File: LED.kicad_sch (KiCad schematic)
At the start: 87 parts

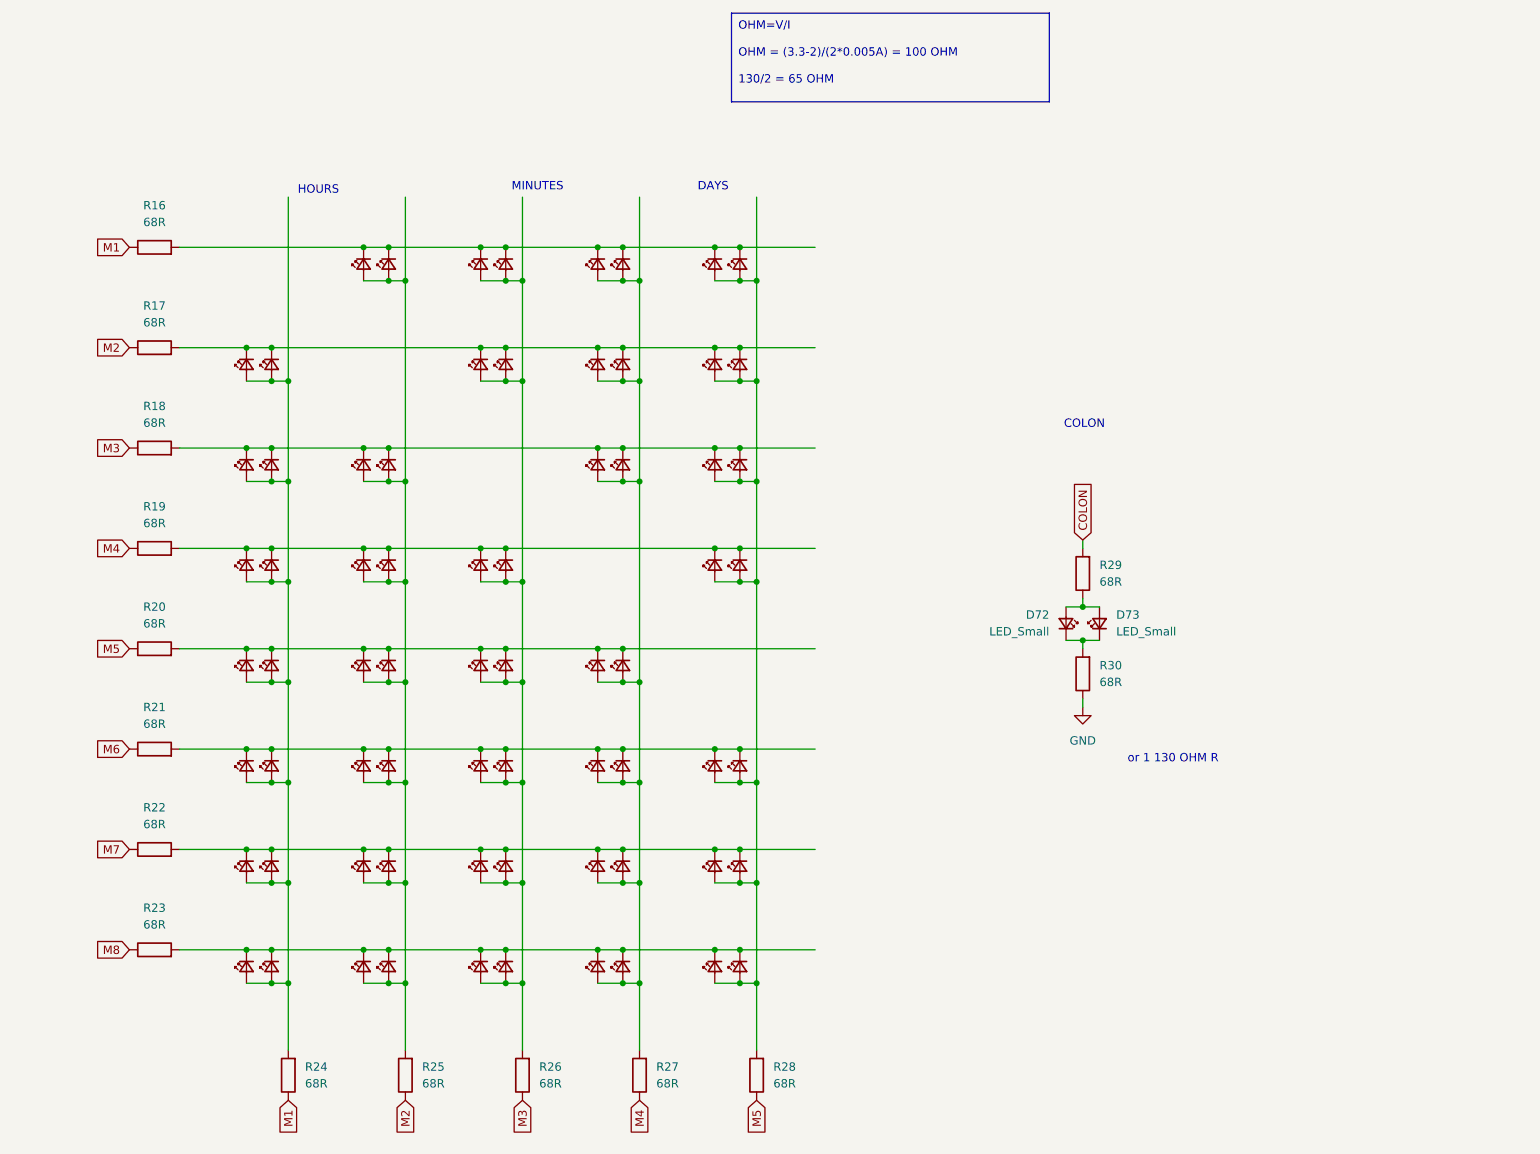
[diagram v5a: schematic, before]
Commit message: charlie plex routing
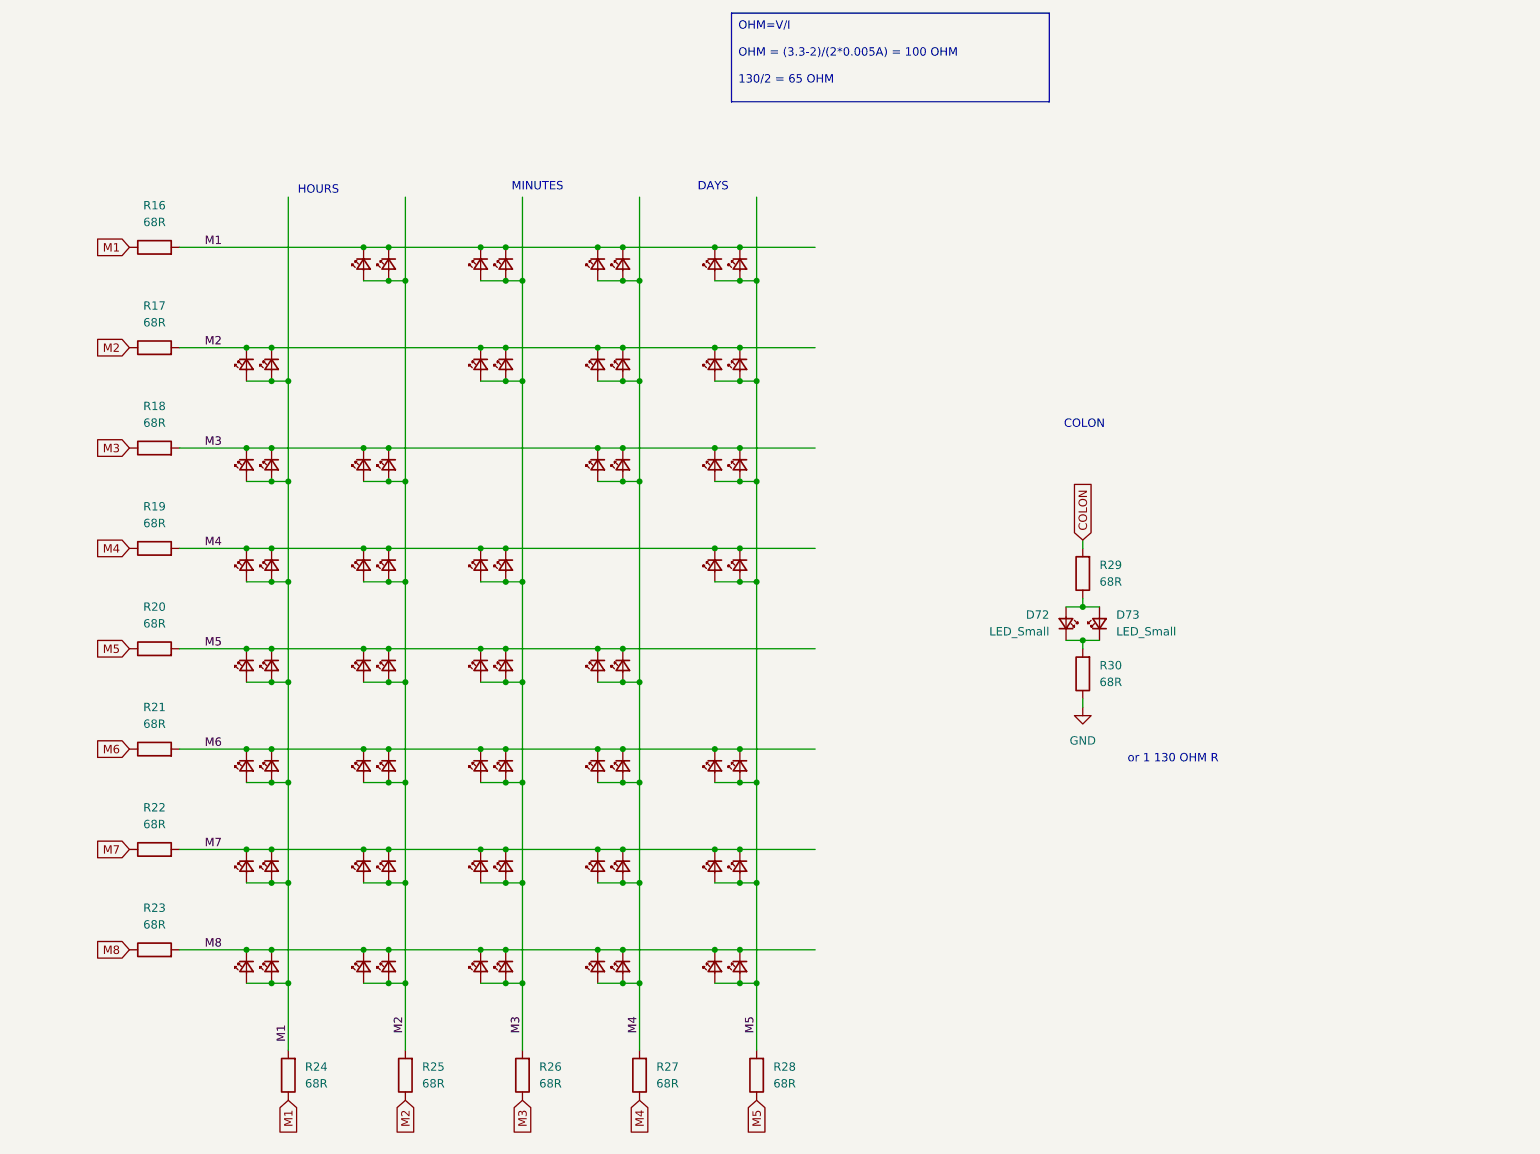
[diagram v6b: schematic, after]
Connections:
- net M1: now also D10.2 (A), D11.2 (A), D12.2 (A), D13.2 (A), D14.2 (A), D15.2 (A), D16.1 (K), D2.2 (A), D23.1 (K), D3.2 (A), D30.1 (K), D37.1 (K), D4.2 (A), D44.1 (K), D5.2 (A), D51.1 (K), D58.1 (K), D6.2 (A), D65.1 (K), D7.2 (A), D8.2 (A), D9.2 (A), R16.2, R24.2
- net M2: now also D16.2 (A), D17.2 (A), D18.2 (A), D19.2 (A), D2.1 (K), D20.2 (A), D21.2 (A), D22.2 (A), D23.2 (A), D24.2 (A), D25.2 (A), D26.2 (A), D27.2 (A), D28.2 (A), D29.2 (A), D31.1 (K), D38.1 (K), D45.1 (K), D52.1 (K), D59.1 (K), D66.1 (K), D9.1 (K), R17.2, R25.2
- net M3: now also D10.1 (K), D17.1 (K), D24.1 (K), D3.1 (K), D30.2 (A), D31.2 (A), D32.2 (A), D33.2 (A), D34.2 (A), D35.2 (A), D36.2 (A), D37.2 (A), D38.2 (A), D39.2 (A), D40.2 (A), D41.2 (A), D42.2 (A), D43.2 (A), D46.1 (K), D53.1 (K), D60.1 (K), D67.1 (K), R18.2, R26.2
- net M4: now also D11.1 (K), D18.1 (K), D25.1 (K), D32.1 (K), D39.1 (K), D4.1 (K), D44.2 (A), D45.2 (A), D46.2 (A), D47.2 (A), D48.2 (A), D49.2 (A), D50.2 (A), D51.2 (A), D52.2 (A), D53.2 (A), D54.2 (A), D55.2 (A), D56.2 (A), D57.2 (A), D61.1 (K), D68.1 (K), R19.2, R27.2
- net M5: now also D12.1 (K), D19.1 (K), D26.1 (K), D33.1 (K), D40.1 (K), D47.1 (K), D5.1 (K), D54.1 (K), D58.2 (A), D59.2 (A), D60.2 (A), D61.2 (A), D62.2 (A), D63.2 (A), D64.2 (A), D65.2 (A), D66.2 (A), D67.2 (A), D68.2 (A), D69.2 (A), D70.2 (A), D71.2 (A), R20.2, R28.2
- net M6: now also D13.1 (K), D20.1 (K), D27.1 (K), D34.1 (K), D41.1 (K), D48.1 (K), D55.1 (K), D6.1 (K), D62.1 (K), D69.1 (K), R21.2
- net M7: now also D14.1 (K), D21.1 (K), D28.1 (K), D35.1 (K), D42.1 (K), D49.1 (K), D56.1 (K), D63.1 (K), D7.1 (K), D70.1 (K), R22.2
- net M8: now also D15.1 (K), D22.1 (K), D29.1 (K), D36.1 (K), D43.1 (K), D50.1 (K), D57.1 (K), D64.1 (K), D71.1 (K), D8.1 (K), R23.2
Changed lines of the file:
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@@
+		)
+	)
+	(label "M4"
+		(at 44.45 96.52 0)
+		(effects
+			(font
+				(size 1.27 1.27)
+			)
+			(justify left bottom)
+		)
+	)
+	(label "M1"
+		(at 57.15 171.45 90)
+		(effects
+			(font
+				(size 1.27 1.27)
+			)
+			(justify left bottom)
+		)
+	)
+	(label "M5"
+		(at 128.27 170.18 90)
+		(effects
+			(font
+				(size 1.27 1.27)
+			)
+			(justify left bottom)
+		)
+	)
+	(label "M8"
+		(at 44.45 157.48 0)
+		(effects
+			(font
+				(size 1.27 1.27)
+			)
+			(justify left bottom)
+		)
+	)
+	(label "M6"
+		(at 44.45 127 0)
+		(effects
+			(font
+				(size 1.27 1.27)
+			)
+			(justify left bottom)
+		)
+	)
+	(label "M4"
+		(at 110.49 170.18 90)
+		(effects
+			(font
+				(size 1.27 1.27)
+			)
+			(justify left bottom)
+		)
+	)
+	(label "M2"
+		(at 44.45 66.04 0)
+		(effects
+			(font
+				(size 1.27 1.27)
+			)
+			(justify left bottom)
+		)
+	)
+	(label "M7"
+		(at 44.45 142.24 0)
+		(effects
+			(font
+				(size 1.27 1.27)
+			)
+			(justify left bottom)
+		)
+	)
+	(label "M1"
+		(at 44.45 50.8 0)
+		(effects
+			(font
+				(size 1.27 1.27)
+			)
+			(justify left bottom)
+		)
+	)
+	(label "M5"
+		(at 44.45 111.76 0)
+		(effects
+			(font
+				(size 1.27 1.27)
+			)
+			(justify left bottom)
+		)
+	)
+	(label "M3"
+		(at 44.45 81.28 0)
+		(effects
+			(font
+				(size 1.27 1.27)
+			)
+			(justify left bottom)
+		)
+	)
+	(label "M3"
+		(at 92.71 170.18 90)
+		(effects
+			(font
+				(size 1.27 1.27)
+			)
+			(justify left bottom)
+		)
+	)
+	(label "M2"
+		(at 74.93 170.18 90)
+		(effects
+			(font
+				(size 1.27 1.27)
+			)
+			(justify left bottom)
 		)
 	)

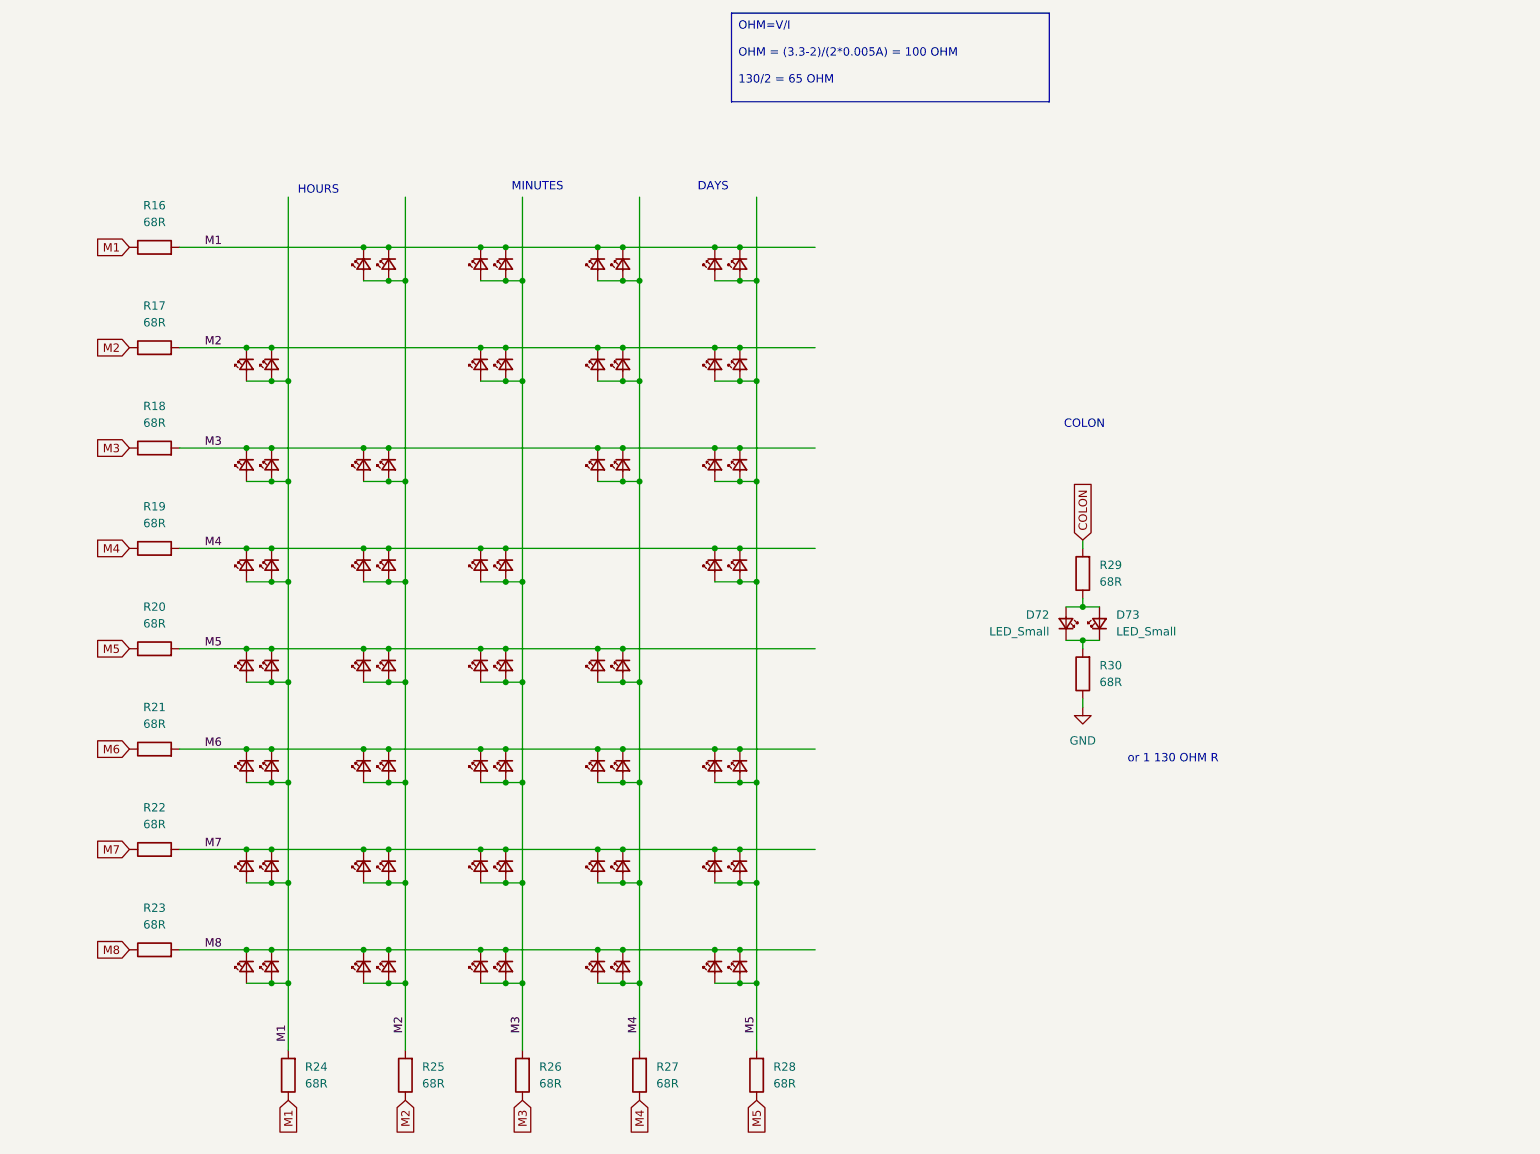
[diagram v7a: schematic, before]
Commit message: all wiring done, need to clean up silk screen edge clips + double check pins for charlieplex & buttons
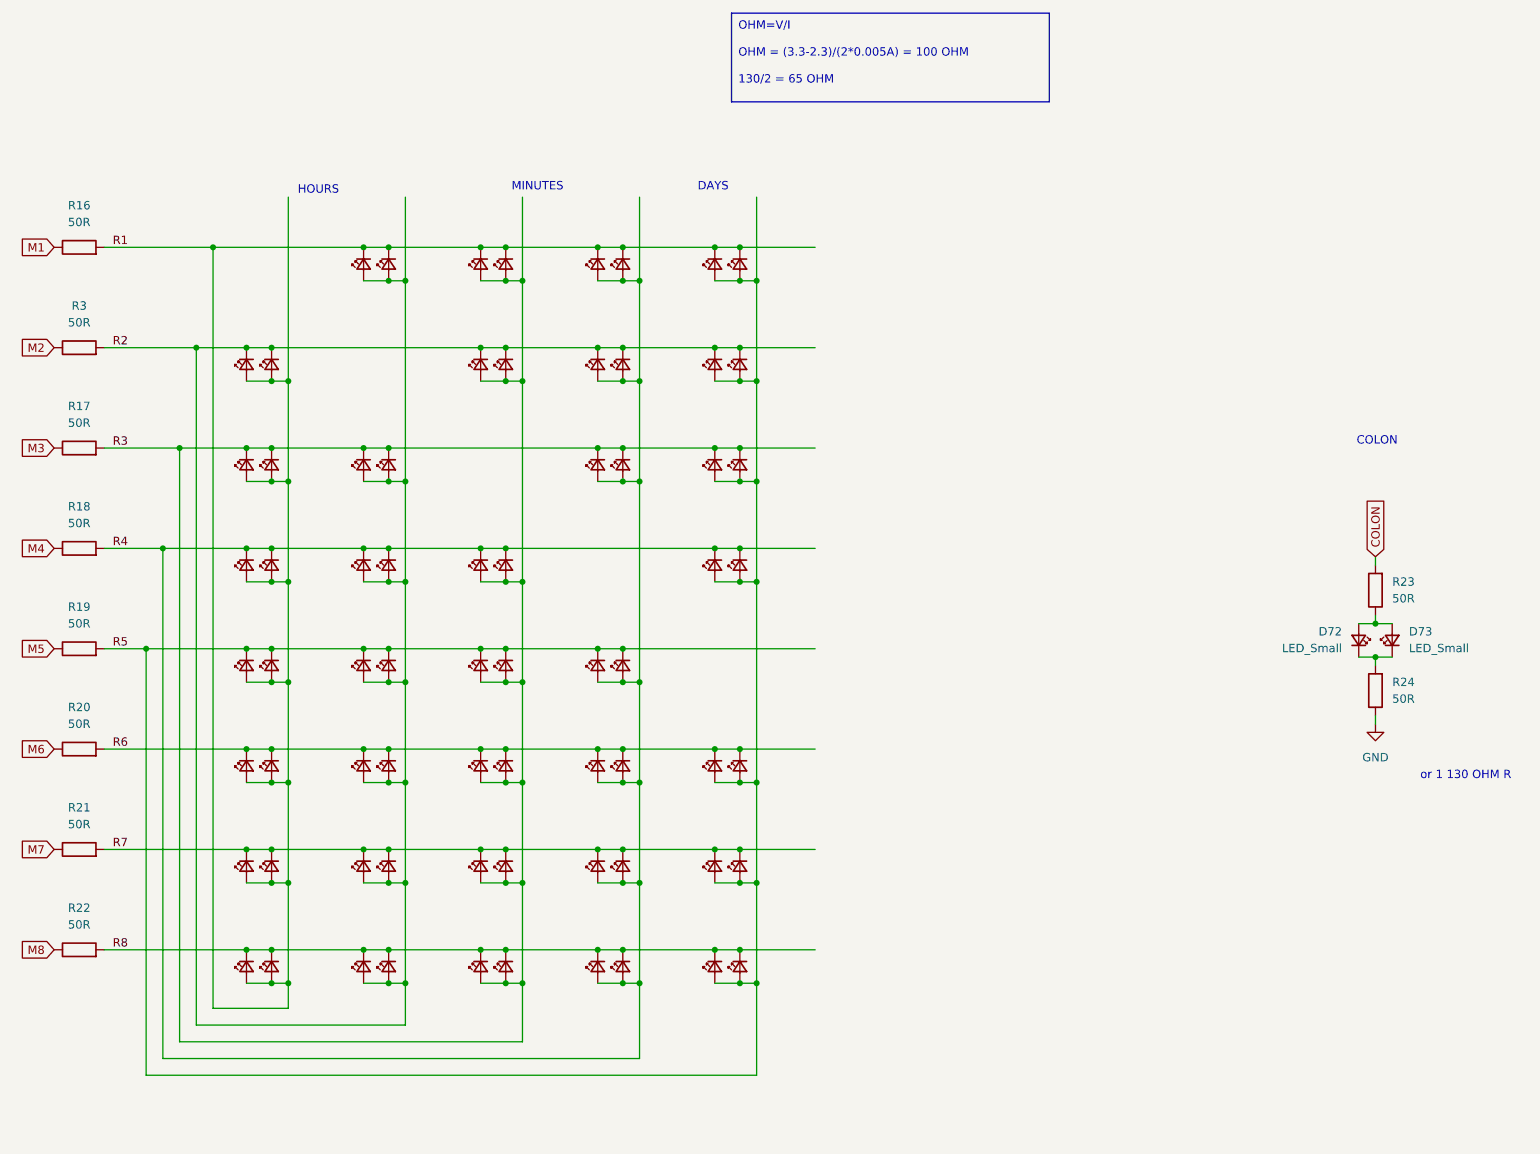
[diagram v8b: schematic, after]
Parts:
- removed R25, R26, R27, R28, R29, R30: 68R, Resistor_SMD:R_0402_1005Metric_Pad0.72x0.64mm_HandSolder, symbol Device:R
- added R3: 50R, Resistor_SMD:R_0402_1005Metric_Pad0.72x0.64mm_HandSolder, symbol Device:R
- R16, R17, R18, R19, R20, R21, R22, R23, R24: value 68R -> 50R
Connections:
- net COLON: now also R23.2
- net GND: now also R24.1
- net M1: no longer D10.2 (A), D11.2 (A), D12.2 (A), D13.2 (A), D14.2 (A), D15.2 (A), D16.1 (K), D2.2 (A), D23.1 (K), D3.2 (A), D30.1 (K), D37.1 (K), D4.2 (A), D44.1 (K), D5.2 (A), D51.1 (K), D58.1 (K), D6.2 (A), D65.1 (K), D7.2 (A), D8.2 (A), D9.2 (A), R16.2, R24.1, R24.2
- net M2: now also R3.1; no longer D16.2 (A), D17.2 (A), D18.2 (A), D19.2 (A), D2.1 (K), D20.2 (A), D21.2 (A), D22.2 (A), D23.2 (A), D24.2 (A), D25.2 (A), D26.2 (A), D27.2 (A), D28.2 (A), D29.2 (A), D31.1 (K), D38.1 (K), D45.1 (K), D52.1 (K), D59.1 (K), D66.1 (K), D9.1 (K), R17.1, R17.2
- net M3: now also R17.1; no longer D10.1 (K), D17.1 (K), D24.1 (K), D3.1 (K), D30.2 (A), D31.2 (A), D32.2 (A), D33.2 (A), D34.2 (A), D35.2 (A), D36.2 (A), D37.2 (A), D38.2 (A), D39.2 (A), D40.2 (A), D41.2 (A), D42.2 (A), D43.2 (A), D46.1 (K), D53.1 (K), D60.1 (K), D67.1 (K), R18.1, R18.2
- net M4: now also R18.1; no longer D11.1 (K), D18.1 (K), D25.1 (K), D32.1 (K), D39.1 (K), D4.1 (K), D44.2 (A), D45.2 (A), D46.2 (A), D47.2 (A), D48.2 (A), D49.2 (A), D50.2 (A), D51.2 (A), D52.2 (A), D53.2 (A), D54.2 (A), D55.2 (A), D56.2 (A), D57.2 (A), D61.1 (K), D68.1 (K), R19.1, R19.2
- net M5: now also R19.1; no longer D12.1 (K), D19.1 (K), D26.1 (K), D33.1 (K), D40.1 (K), D47.1 (K), D5.1 (K), D54.1 (K), D58.2 (A), D59.2 (A), D60.2 (A), D61.2 (A), D62.2 (A), D63.2 (A), D64.2 (A), D65.2 (A), D66.2 (A), D67.2 (A), D68.2 (A), D69.2 (A), D70.2 (A), D71.2 (A), R20.1, R20.2
- net M6: now also R20.1; no longer D13.1 (K), D20.1 (K), D27.1 (K), D34.1 (K), D41.1 (K), D48.1 (K), D55.1 (K), D6.1 (K), D62.1 (K), D69.1 (K), R21.1, R21.2
- net M7: now also R21.1; no longer D14.1 (K), D21.1 (K), D28.1 (K), D35.1 (K), D42.1 (K), D49.1 (K), D56.1 (K), D63.1 (K), D7.1 (K), D70.1 (K), R22.1, R22.2
- net M8: now also R22.1; no longer D15.1 (K), D22.1 (K), D29.1 (K), D36.1 (K), D43.1 (K), D50.1 (K), D57.1 (K), D64.1 (K), D71.1 (K), D8.1 (K), R23.1, R23.2
- net at D72.1 (K), D73.1 (K): now also R24.2
- net at D72.2 (A), D73.2 (A): now also R23.1
- new net R1: D10.2 (A), D11.2 (A), D12.2 (A), D13.2 (A), D14.2 (A), D15.2 (A), D16.1 (K), D2.2 (A), D23.1 (K), D3.2 (A), D30.1 (K), D37.1 (K), D4.2 (A), D44.1 (K), D5.2 (A), D51.1 (K), D58.1 (K), D6.2 (A), D65.1 (K), D7.2 (A), D8.2 (A), D9.2 (A), R16.2
- new net R2: D16.2 (A), D17.2 (A), D18.2 (A), D19.2 (A), D2.1 (K), D20.2 (A), D21.2 (A), D22.2 (A), D23.2 (A), D24.2 (A), D25.2 (A), D26.2 (A), D27.2 (A), D28.2 (A), D29.2 (A), D31.1 (K), D38.1 (K), D45.1 (K), D52.1 (K), D59.1 (K), D66.1 (K), D9.1 (K), R3.2
- new net R3: D10.1 (K), D17.1 (K), D24.1 (K), D3.1 (K), D30.2 (A), D31.2 (A), D32.2 (A), D33.2 (A), D34.2 (A), D35.2 (A), D36.2 (A), D37.2 (A), D38.2 (A), D39.2 (A), D40.2 (A), D41.2 (A), D42.2 (A), D43.2 (A), D46.1 (K), D53.1 (K), D60.1 (K), D67.1 (K), R17.2
- new net R4: D11.1 (K), D18.1 (K), D25.1 (K), D32.1 (K), D39.1 (K), D4.1 (K), D44.2 (A), D45.2 (A), D46.2 (A), D47.2 (A), D48.2 (A), D49.2 (A), D50.2 (A), D51.2 (A), D52.2 (A), D53.2 (A), D54.2 (A), D55.2 (A), D56.2 (A), D57.2 (A), D61.1 (K), D68.1 (K), R18.2
- new net R5: D12.1 (K), D19.1 (K), D26.1 (K), D33.1 (K), D40.1 (K), D47.1 (K), D5.1 (K), D54.1 (K), D58.2 (A), D59.2 (A), D60.2 (A), D61.2 (A), D62.2 (A), D63.2 (A), D64.2 (A), D65.2 (A), D66.2 (A), D67.2 (A), D68.2 (A), D69.2 (A), D70.2 (A), D71.2 (A), R19.2
- new net R6: D13.1 (K), D20.1 (K), D27.1 (K), D34.1 (K), D41.1 (K), D48.1 (K), D55.1 (K), D6.1 (K), D62.1 (K), D69.1 (K), R20.2
- new net R7: D14.1 (K), D21.1 (K), D28.1 (K), D35.1 (K), D42.1 (K), D49.1 (K), D56.1 (K), D63.1 (K), D7.1 (K), D70.1 (K), R21.2
- new net R8: D15.1 (K), D22.1 (K), D29.1 (K), D36.1 (K), D43.1 (K), D50.1 (K), D57.1 (K), D64.1 (K), D71.1 (K), D8.1 (K), R22.2
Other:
- moved on the sheet: D72, D73, R16
